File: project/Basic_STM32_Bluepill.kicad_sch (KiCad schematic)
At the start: 32 parts, among them J1 Conn_01x04_Pin, J2 Conn_01x04_Pin, J3 USB_B_Micro, J4 Conn_01x04_Pin, SW1 SW_SPDT, U1 AMS1117-3.3, U2 STM32F103C8T6, Y1 16 MHz

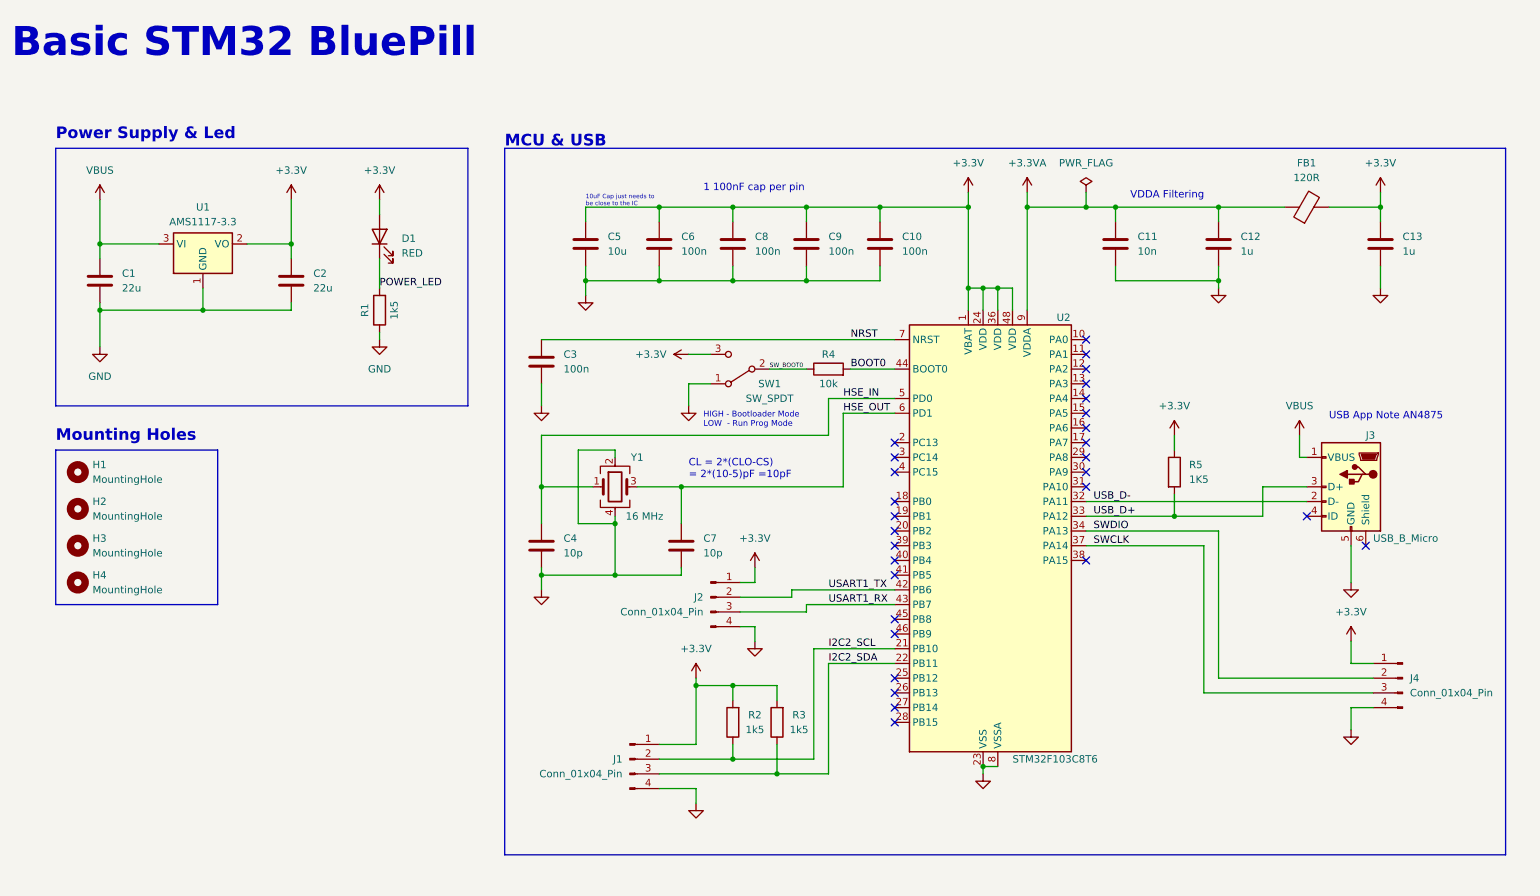
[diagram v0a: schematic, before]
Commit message: First draft of changes
Added the RPi style connector and an extra for remaining pins.
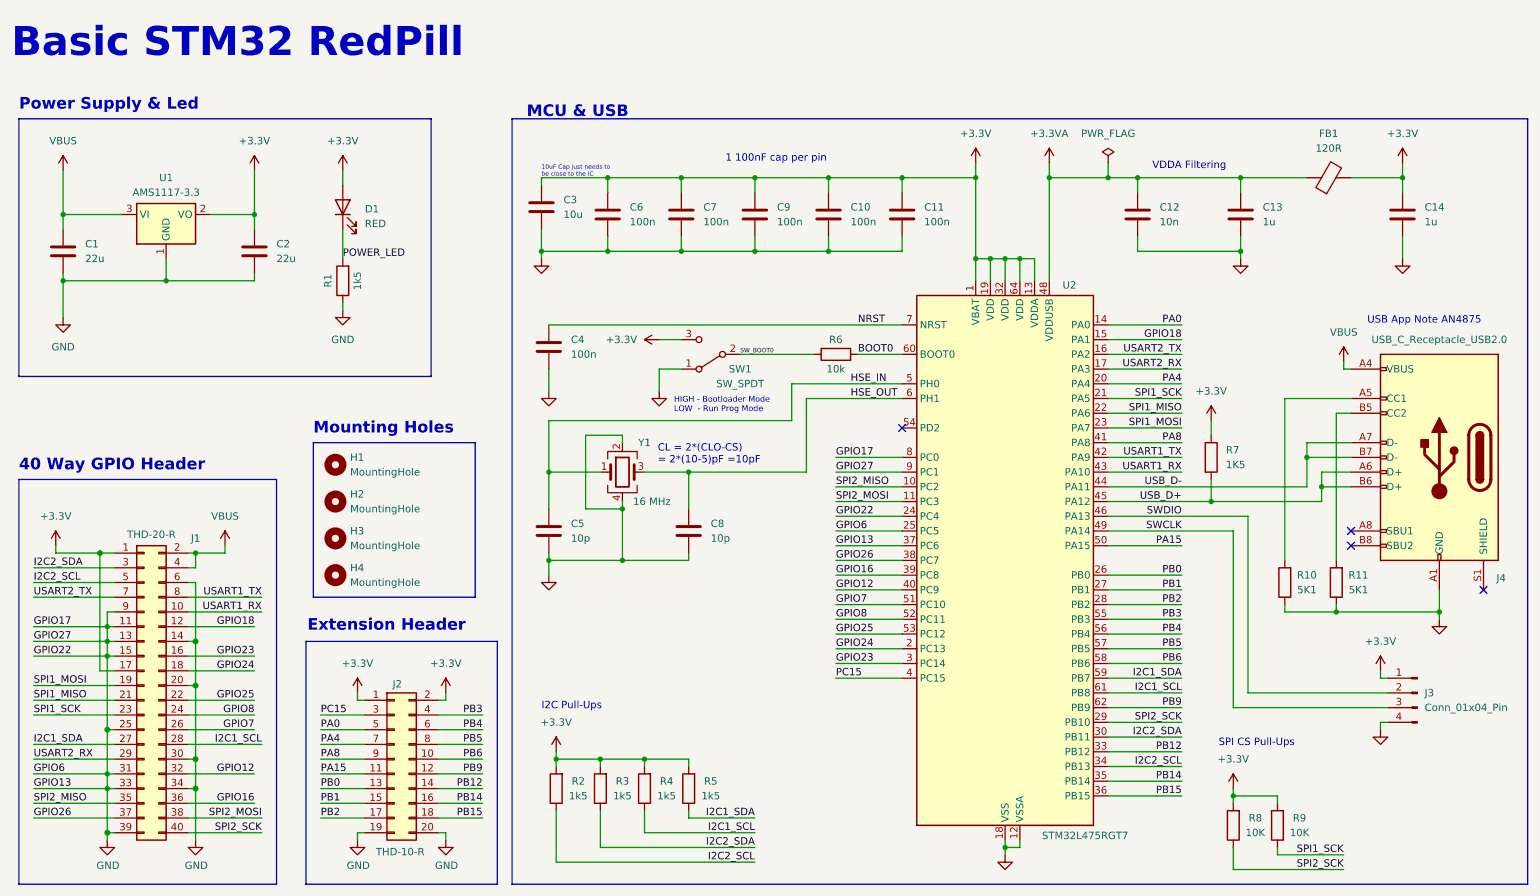
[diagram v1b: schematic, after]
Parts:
- removed J1, J2: Conn_01x04_Pin, Connector_PinHeader_2.54mm:PinHeader_1x04_P2.54mm_Vertical, symbol Connector:Conn_01x04_Pin
- removed J3: USB_B_Micro, Connector_USB:USB_Micro-B_Wuerth_629105150521, symbol Connector:USB_B_Micro
- added C6: 100n, Capacitor_SMD:C_0402_1005Metric, symbol Device:C
- added J1: THD-20-R, Connector_PinHeader_2.54mm:PinHeader_2x20_P2.54mm_Vertical, symbol Connector_Generic:Conn_02x20_Odd_Even
- added J2: THD-10-R, Connector_PinHeader_2.54mm:PinHeader_2x10_P2.54mm_Vertical, symbol Connector_Generic:Conn_02x10_Odd_Even
- added J4: USB_C_Receptacle_USB2.0, Connector_USB:USB_C_Receptacle_GCT_USB4105-xx-A_16P_TopMnt_Horizontal, symbol Connector:USB_C_Receptacle_USB2.0_16P
- added R10, R11: 5K1, Resistor_SMD:R_0402_1005Metric, symbol Device:R
- added R2, R3: 1k5, Resistor_SMD:R_0402_1005Metric, symbol Device:R
- added R8, R9: 10K, Resistor_SMD:R_0402_1005Metric, symbol Device:R
- U2: value STM32F103C8T6 -> STM32L475RGT7; footprint Package_QFP:LQFP-48_7x7mm_P0.5mm -> Package_QFP:LQFP-64_10x10mm_P0.5mm; symbol MCU_ST_STM32F1:STM32F103C8Tx -> MCU_ST_STM32L4:STM32L475RGTx
- renumbered C9 to C10, C10 to C11, C11 to C12, C12 to C13, C13 to C14, C5 to C3, C3 to C4, C4 to C5, C6 to C7, C7 to C8, C8 to C9, J4 to J3, R2 to R4, R3 to R5, R4 to R6, R5 to R7
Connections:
- net +3.3V: now also U2.13 (VDDA), U2.19 (VDD), U2.32 (VDD), U2.64 (VDD), C6.1, J1.1 (Pin_1), J1.17 (Pin_17), J2.1 (Pin_1), J2.2 (Pin_2), R2.2, R3.2, R8.2, R9.2; no longer U2.24 (VDD), U2.36 (VDD), U2.48 (VDD)
- net +3.3VA: now also U2.48 (VDDUSB); no longer U2.9 (VDDA)
- net BOOT0: now also U2.60 (BOOT0); no longer U2.44 (BOOT0)
- net GND: now also U2.12 (VSSA), U2.18 (VSS), U2.24 (PC4), U2.25 (PC5), U2.31 (VSS), U2.37 (PC6), U2.63 (VSS), U2.9 (PC1), C6.2, J1.11 (Pin_11), J1.13 (Pin_13), J1.14 (Pin_14), J1.15 (Pin_15), J1.20 (Pin_20), J1.25 (Pin_25), J1.30 (Pin_30), J1.31 (Pin_31), J1.33 (Pin_33), J1.34 (Pin_34), J1.39 (Pin_39), J1.6 (Pin_6), J1.9 (Pin_9), J2.19 (Pin_19), J2.20 (Pin_20), J4.A1 (GND), J4.A12 (GND), J4.B1 (GND), J4.B12 (GND), R10.1, R11.1; no longer U2.23 (VSS), U2.35 (VSS)
- net I2C2_SCL: now also U2.34 (PB13), J1.5 (Pin_5), R2.1; no longer R4.1, U2.21 (PB10)
- net I2C2_SDA: now also U2.30 (PB11), J1.3 (Pin_3), R3.1; no longer R5.1, U2.22 (PB11)
- net SWCLK: now also U2.49 (PA14); no longer U2.37 (PA14)
- net SWDIO: now also U2.46 (PA13); no longer U2.34 (PA13)
- net USART1_RX: now also J1.10 (Pin_10)
- net USART1_TX: now also J1.8 (Pin_8)
- net USB_D+: now also U2.45 (PA12), J4.A6 (D+), J4.B6 (D+); no longer U2.33 (PA12)
- net USB_D-: now also U2.44 (PA11), J4.A7 (D-), J4.B7 (D-); no longer U2.32 (PA11)
- net VBUS: now also J1.2 (Pin_2), J1.4 (Pin_4), J4.A4 (VBUS), J4.A9 (VBUS), J4.B4 (VBUS), J4.B9 (VBUS)
- net SPI2_MISO: now reaches U2.10 (PC2)
- net SPI2_MISO: now also J1.35 (Pin_35)
- net SPI2_MOSI: now reaches U2.11 (PC3)
- net SPI2_MOSI: now also J1.38 (Pin_38)
- net PA0: now reaches U2.14 (PA0)
- net PA0: now also J2.5 (Pin_5)
- net GPIO18: now reaches U2.15 (PA1)
- net GPIO18: now also J1.12 (Pin_12)
- net USART2_TX: now reaches U2.16 (PA2)
- net USART2_TX: now also J1.7 (Pin_7)
- net USART2_RX: now reaches U2.17 (PA3)
- net USART2_RX: now also J1.29 (Pin_29)
- net GPIO24: now reaches U2.2 (PC13)
- net GPIO24: now also J1.18 (Pin_18)
- net PA4: now reaches U2.20 (PA4)
- net PA4: now also J2.7 (Pin_7)
- net PB0: now reaches U2.26 (PB0)
- net PB0: now also J2.13 (Pin_13)
- net PB1: now reaches U2.27 (PB1)
- net PB1: now also J2.15 (Pin_15)
- net PB2: now reaches U2.28 (PB2)
- net PB2: now also J2.17 (Pin_17)
- net SPI2_SCK: now reaches U2.29 (PB10)
- net SPI2_SCK: now also J1.40 (Pin_40), R8.1
- net GPIO23: now reaches U2.3 (PC14)
- net GPIO23: now also J1.16 (Pin_16)
- net GPIO26: now reaches U2.38 (PC7)
- net GPIO26: now also J1.37 (Pin_37)
- net GPIO16: now reaches U2.39 (PC8)
- net GPIO16: now also J1.36 (Pin_36)
- net PC15: now reaches U2.4 (PC15)
- net PC15: now also J2.3 (Pin_3)
- net GPIO12: now reaches U2.40 (PC9)
- net GPIO12: now also J1.32 (Pin_32)
- net PA8: now reaches U2.41 (PA8)
- net PA8: now also J2.9 (Pin_9)
- new net: J4.A5 (CC1), R10.2
- new net: J4.B5 (CC2), R11.2
- new net GPIO25: J1.22 (Pin_22), U2.53 (PC12)
- new net GPIO7: J1.26 (Pin_26), U2.51 (PC10)
- new net GPIO8: J1.24 (Pin_24), U2.52 (PC11)
- new net I2C1_SCL: J1.28 (Pin_28), R4.1, U2.61 (PB8)
- new net I2C1_SDA: J1.27 (Pin_27), R5.1, U2.59 (PB7)
- new net PA15: J2.11 (Pin_11), U2.50 (PA15)
- new net PB12: J2.14 (Pin_14), U2.33 (PB12)
- new net PB14: J2.16 (Pin_16), U2.35 (PB14)
- new net PB15: J2.18 (Pin_18), U2.36 (PB15)
- new net PB3: J2.4 (Pin_4), U2.55 (PB3)
- new net PB4: J2.6 (Pin_6), U2.56 (PB4)
- new net PB5: J2.8 (Pin_8), U2.57 (PB5)
- new net PB6: J2.10 (Pin_10), U2.58 (PB6)
- new net PB9: J2.12 (Pin_12), U2.62 (PB9)
- new net SPI1_MISO: J1.21 (Pin_21), U2.22 (PA6)
- new net SPI1_MOSI: J1.19 (Pin_19), U2.23 (PA7)
- new net SPI1_SCK: J1.23 (Pin_23), R9.1, U2.21 (PA5)
- no-connect marks 29 -> 4
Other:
- note added: "40 Way GPIO Header"
- note added: "Basic STM32 RedPill"
- note added: "Extension Header"
- note added: "I2C Pull-Ups"
- note added: "SPI CS Pull-Ups"
- note removed: "Basic STM32 BluePill"
- company: SY -> ADS
- title: Basic STM32 Bluepill -> Basic STM32 Redpill
- moved on the sheet: C1, C10, C11, C12, C13, C14, C2, C3, C4, C5, C7, C8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
